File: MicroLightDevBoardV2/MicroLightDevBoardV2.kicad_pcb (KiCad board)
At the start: 2 copper layers, 81.5 x 75.9 mm, 77 parts, among them J1 Conn_01x05_Socket, J10 Conn_01x02_Socket, J11 Conn_01x05_Socket, J12 Conn_01x02_Socket, J13 Conn_01x04_Socket, J14 Conn_01x04_Socket, J15 Conn_01x05_Socket, J16 Conn_01x01_Socket, J17 Conn_01x04_Socket, J18 Conn_01x02_Socket, J19 Conn_01x02_Socket, J2 Conn_01x05_Socket, J20 Conn_01x03_Socket, J21 Conn_01x03_Socket, J22 Conn_01x02_Socket, J23 Conn_01x02_Socket, J24 Conn_01x02_Socket, J25 Conn_01x02_Socket, J26 Conn_01x01_Socket, J27 Conn_01x06_Socket, J28 Conn_01x04_Socket, J29 Conn_01x04_Socket, J3 Conn_01x05_Socket, J30 Conn_01x04_Socket, J31 Conn_01x04_Socket, J32 Conn_01x04_Socket, J33 Conn_01x04_Socket, J34 Conn_01x04_Socket, J35 Conn_01x04_Socket, J36 Conn_01x04_Socket, J37 Conn_01x04_Socket, J38 Conn_01x04_Socket, J39 Conn_01x04_Socket, J4 Conn_01x05_Socket, J40 Conn_01x04_Socket, J41 Conn_01x04_Socket, J42 Conn_01x04_Socket, J43 Conn_01x04_Socket, J5 Conn_01x02_Socket, J6 Conn_01x02_Socket, J7 TYPE-C-31-M-12, J8 Conn_01x02_Socket, J9 Conn_01x02_Socket, U1 BQ25628RYKR, U2 ATtiny3226-M, U3 S-85S1AB33-I6T1U, U4 B3U-1000P, U5 B3U-1000P, U6 USBLC6-2P6, U7 MC3479

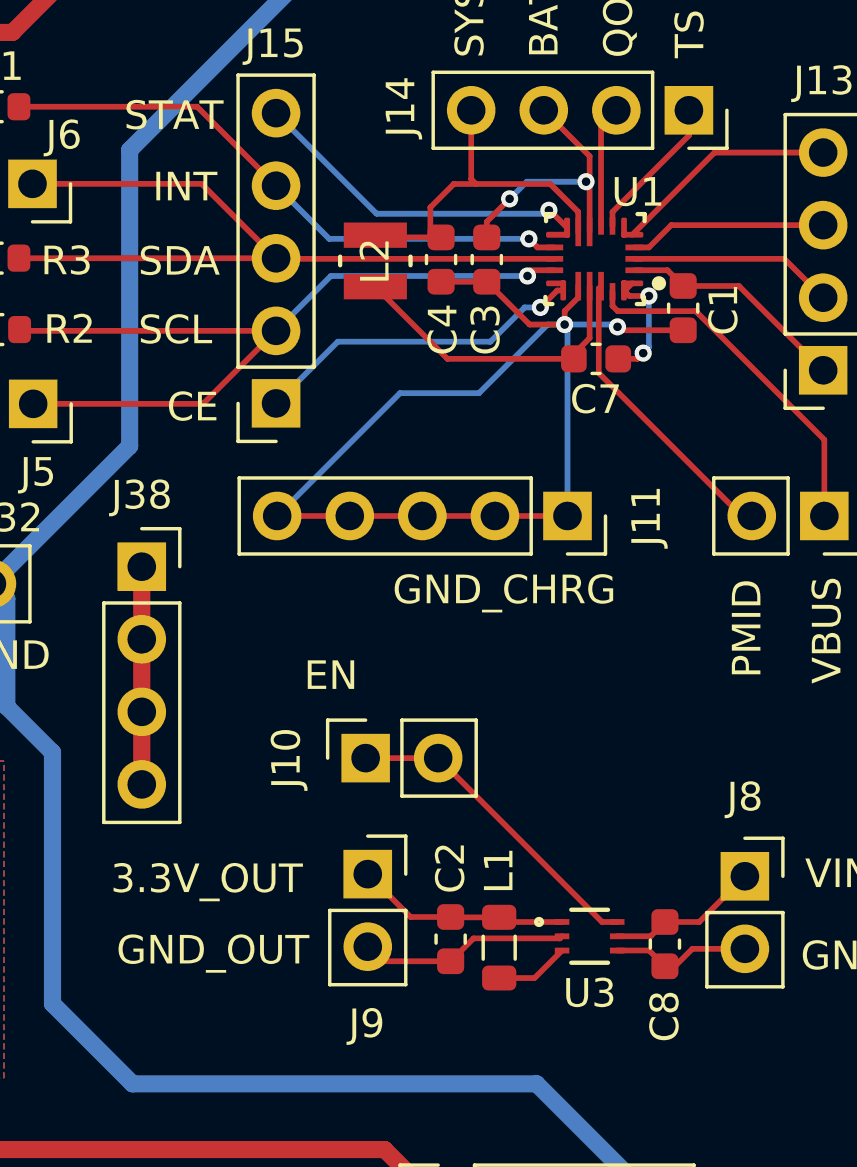
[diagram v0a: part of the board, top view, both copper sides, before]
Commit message: added 2.2uh power inductor from wurth, updated first inductor footprint
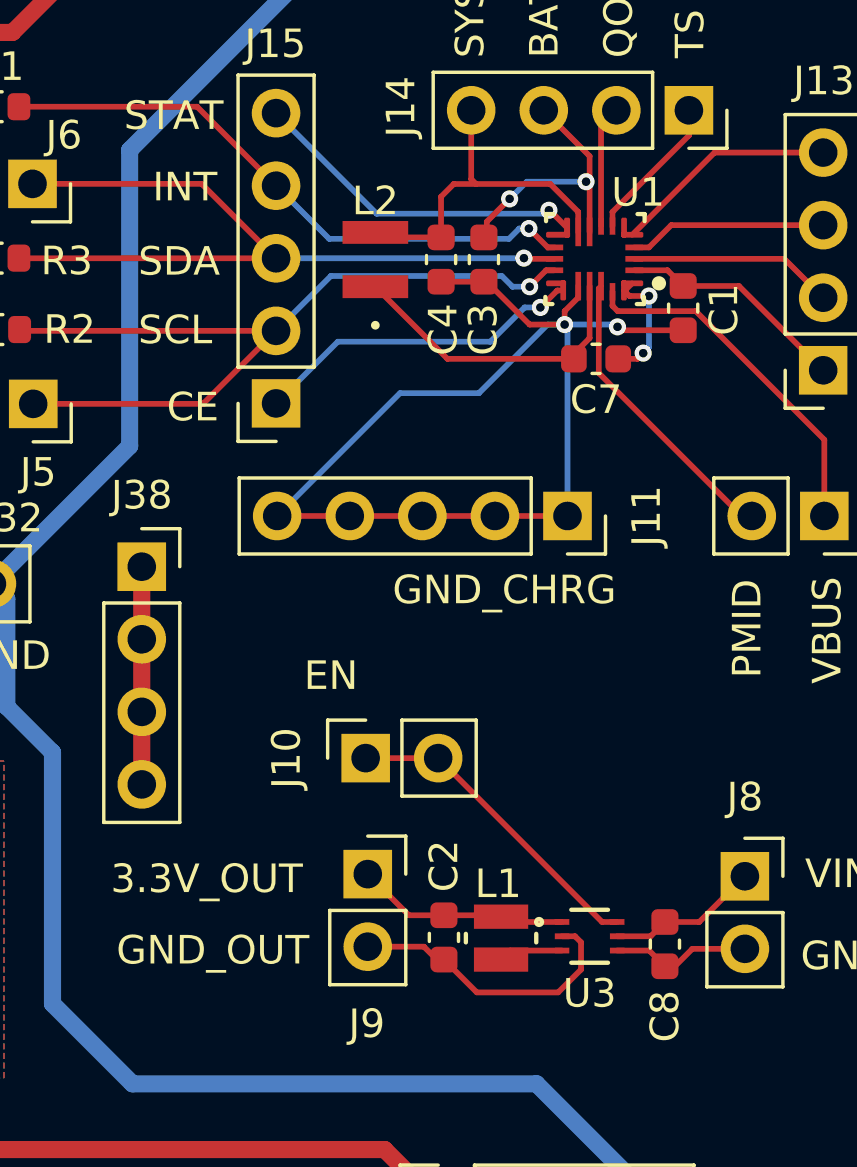
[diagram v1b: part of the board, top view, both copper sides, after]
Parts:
- L1: footprint Inductor_SMD:L_0805_2012Metric -> MicroLightDevBoard:74438343022_L
- L2: footprint MicroLightDevBoard:IND_2508-WE-MAPI_WRE -> MicroLightDevBoard:74438322010_L
- moved L1 0.34 mm to (178.6, 90.3)
- moved C2 0.24 mm to (176.6, 90.3)
- moved C3 0.10 mm to (178.0, 66.5)
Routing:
- net GND_3V3: track 7.37 -> 10.2 mm
- net SDA_CHRG: vias 0 -> 1

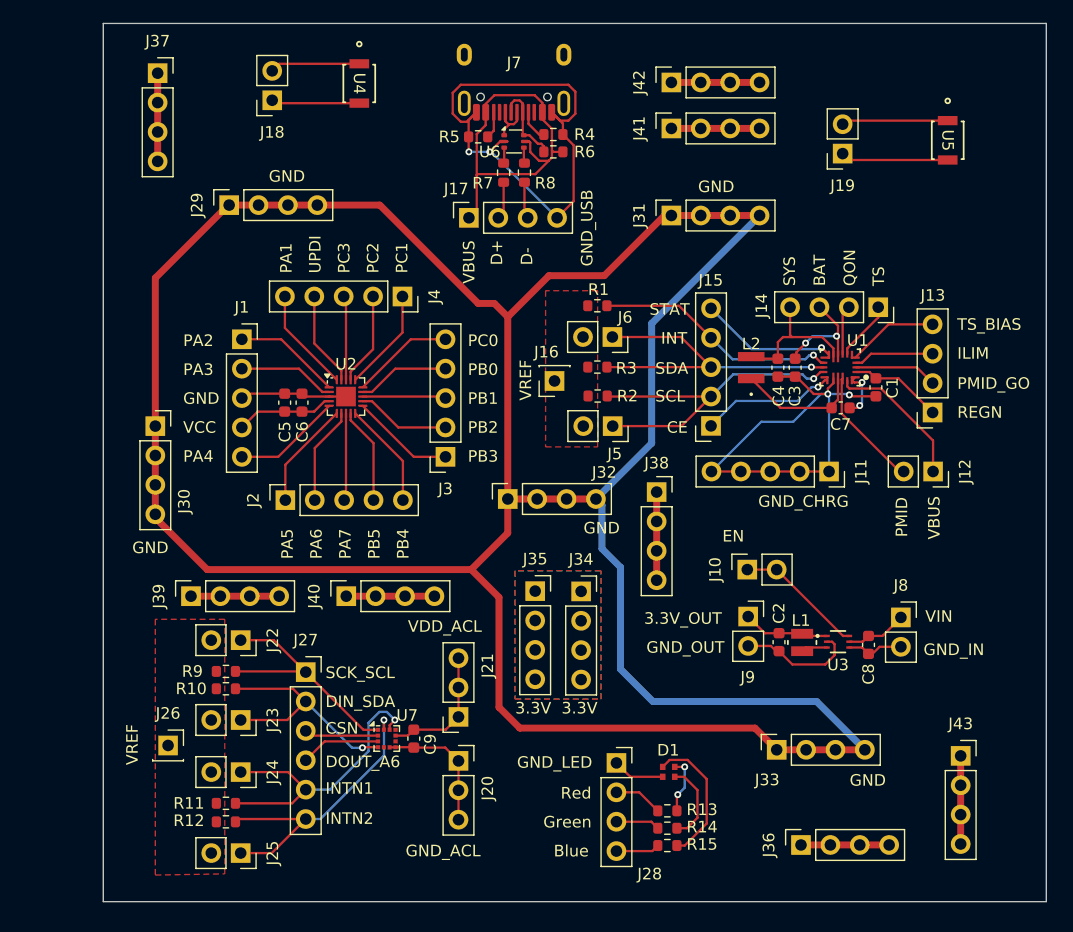
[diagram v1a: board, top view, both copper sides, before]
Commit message: adding lcsc part numbers, and more unconnected breakouts
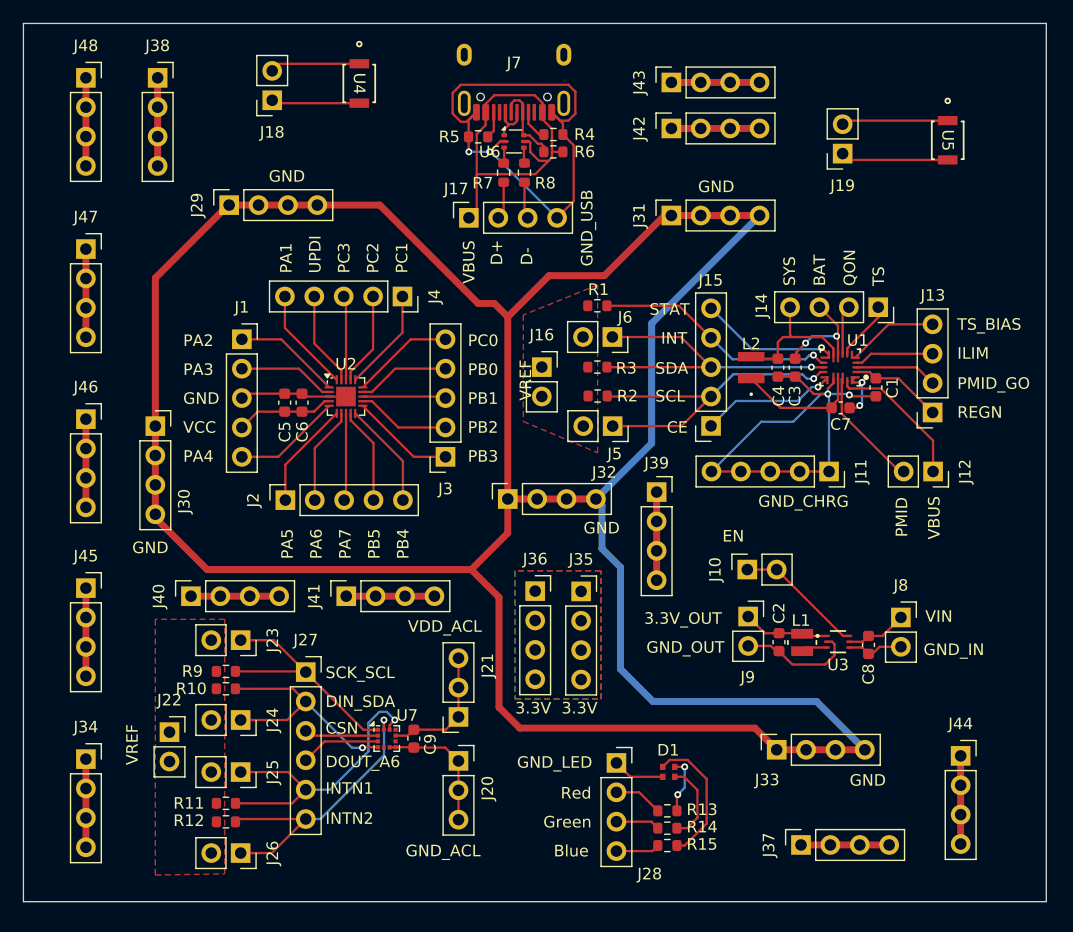
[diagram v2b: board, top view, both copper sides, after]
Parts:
- removed the J26 at (123.8, 99.2)
- added J22: Conn_01x02_Socket, Connector_PinSocket_2.54mm:PinSocket_1x02_P2.54mm_Vertical, F.Cu at (123.9, 98.0)
- added J34: Conn_01x04_Socket, Connector_PinSocket_2.54mm:PinSocket_1x04_P2.54mm_Vertical, F.Cu at (116.7, 100.4)
- added J45: Conn_01x04_Socket, Connector_PinSocket_2.54mm:PinSocket_1x04_P2.54mm_Vertical, F.Cu at (116.7, 85.6)
- added J46: Conn_01x04_Socket, Connector_PinSocket_2.54mm:PinSocket_1x04_P2.54mm_Vertical, F.Cu at (116.7, 71.0)
- added J47: Conn_01x04_Socket, Connector_PinSocket_2.54mm:PinSocket_1x04_P2.54mm_Vertical, F.Cu at (116.7, 56.3)
- added J48: Conn_01x04_Socket, Connector_PinSocket_2.54mm:PinSocket_1x04_P2.54mm_Vertical, F.Cu at (116.7, 41.5)
- J16: value Conn_01x01_Socket -> Conn_01x02_Socket; footprint Connector_PinSocket_2.54mm:PinSocket_1x01_P2.54mm_Vertical -> Connector_PinSocket_2.54mm:PinSocket_1x02_P2.54mm_Vertical
- moved J16 1.63 mm to (156.1, 66.5), turned to 0 degrees
- moved J38 0.40 mm to (122.9, 41.5)
- renumbered J22 to J23, J23 to J24, J24 to J25, J25 to J26, J34 to J35, J35 to J36, J36 to J37, J37 to J38, J38 to J39, J39 to J40, J40 to J41, J41 to J42, J42 to J43, J43 to J44
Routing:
- net Net-(J47-Pin_1): track 0.00 -> 7.62 mm
- net Net-(J46-Pin_1): track 0.00 -> 7.62 mm
- net Net-(J45-Pin_1): track 0.00 -> 7.62 mm
- net Net-(J34-Pin_1): track 0.00 -> 7.62 mm
- net Net-(J48-Pin_1): track 0.00 -> 7.62 mm
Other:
- board size 81.5 x 75.9 mm -> 88.4 x 75.9 mm

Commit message: cleaning up and adding connectors
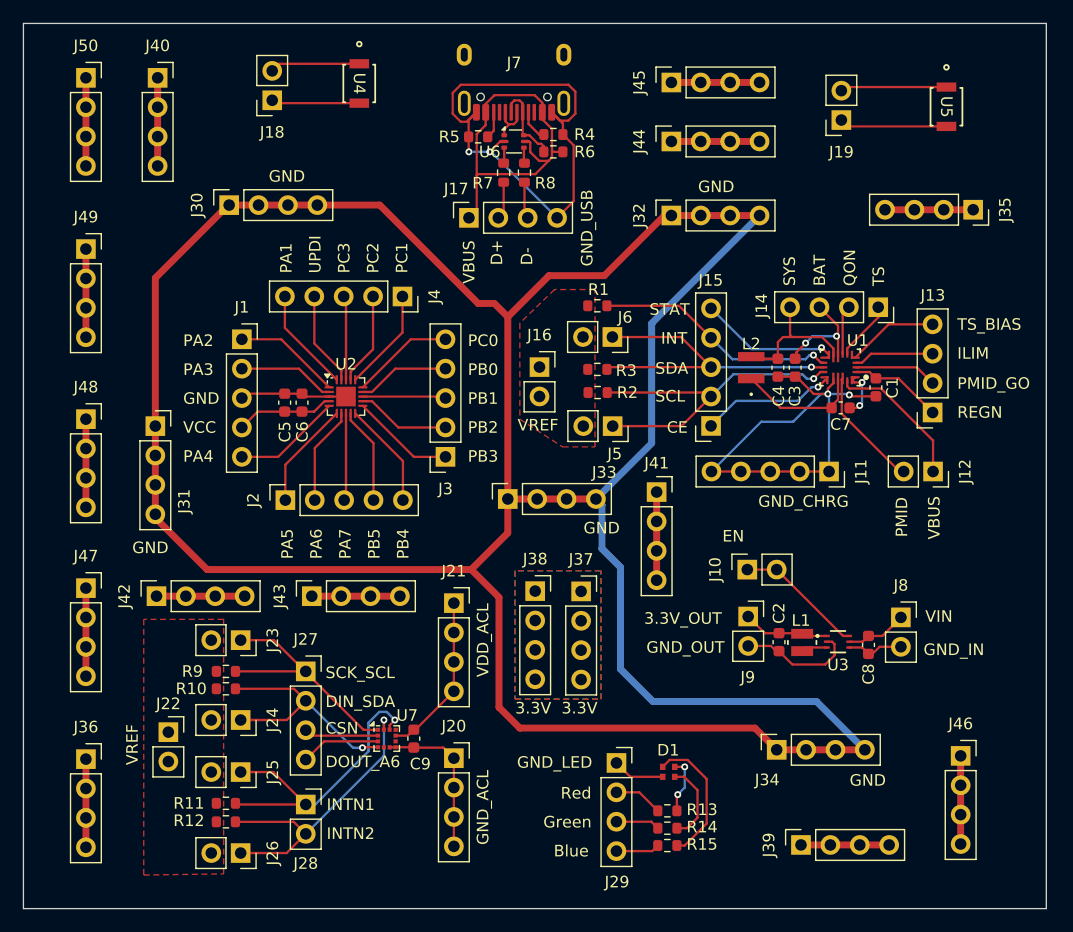
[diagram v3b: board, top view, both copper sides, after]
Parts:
- added J28: Conn_01x02_Socket, Connector_PinSocket_2.54mm:PinSocket_1x02_P2.54mm_Vertical, F.Cu at (135.7, 104.3)
- added J35: Conn_01x04_Socket, Connector_PinSocket_2.54mm:PinSocket_1x04_P2.54mm_Vertical, F.Cu at (193.4, 52.9)
- J20, J21: value Conn_01x03_Socket -> Conn_01x04_Socket; footprint Connector_PinSocket_2.54mm:PinSocket_1x03_P2.54mm_Vertical -> Connector_PinSocket_2.54mm:PinSocket_1x04_P2.54mm_Vertical
- J27: value Conn_01x06_Socket -> Conn_01x04_Socket; footprint Connector_PinSocket_2.54mm:PinSocket_1x06_P2.54mm_Vertical -> Connector_PinSocket_2.54mm:PinSocket_1x04_P2.54mm_Vertical
- moved J21 9.84 mm to (148.5, 86.9), turned to 0 degrees
- moved J42 2.98 mm to (122.8, 86.3)
- moved J43 2.98 mm to (136.2, 86.3)
- moved J19 2.90 mm to (182.0, 45.2)
- moved U5 2.90 mm to (191.1, 44.0)
- moved J44 1.12 mm to (167.3, 47.0)
- moved J20 0.46 mm to (148.5, 100.3)
- moved R2 0.30 mm to (160.9, 68.7)
- moved R3 0.20 mm to (160.9, 66.7)
- moved J16 0.20 mm to (155.9, 66.5)
- moved J22 0.10 mm to (123.8, 98.0)
- moved J27 0.06 mm to (135.7, 92.8)
- renumbered J28 to J29, J29 to J30, J30 to J31, J31 to J32, J32 to J33, J33 to J34, J34 to J36, J35 to J37, J36 to J38, J37 to J39, J38 to J40, J39 to J41, J40 to J42, J41 to J43, J42 to J44, J43 to J45, J44 to J46, J45 to J47, J46 to J48, J47 to J49, J48 to J50
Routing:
- net Net-(J35-Pin_1): track 0.00 -> 7.62 mm
- net VDD_ACL: track 11.2 -> 14.2 mm
- net GND_ACL: track 11.5 -> 13.6 mm
- net INTN1_ACL: track 26.1 -> 26.7 mm
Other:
- board size 88.4 x 75.9 mm -> 88.4 x 76.5 mm
